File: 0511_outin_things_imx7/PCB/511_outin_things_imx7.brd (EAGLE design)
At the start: 85 x 56 mm, 57 parts

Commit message: Update for android things.
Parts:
- moved JP1 1.27 mm to (52.1, 37.0)
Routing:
- net 5V: track 275.3 -> 303.2 mm, vias 1 -> 0
- net N$7: track 35.5 -> 61.2 mm, vias 2 -> 0
- net GND: track 356.1 -> 375.5 mm, vias 21 -> 10
- net LED5: track 17.7 -> 36.1 mm, vias 2 -> 0
- net N$14: track 42.4 -> 28.5 mm, vias 2 -> 4
- net MOSI: track 37.1 -> 50.2 mm
- net SDA: track 62.9 -> 54.4 mm, vias 1 -> 0
- net CH1: track 31.7 -> 39.5 mm
- net MISO: track 45.4 -> 39.5 mm, vias 0 -> 1
- net I2S_SDOUT: track 40.5 -> 34.9 mm
- net CH0: track 40.1 -> 43.4 mm
- net SCL: track 49.0 -> 52.0 mm
- net LED3: track 14.7 -> 17.6 mm, vias 0 -> 2
- net SCLK: track 45.0 -> 42.3 mm
- net I2S_SDIN: track 29.8 -> 32.4 mm
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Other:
- board text added: "Rev.1.0.0D"
- board text removed: "Rev.1.0.0 C"

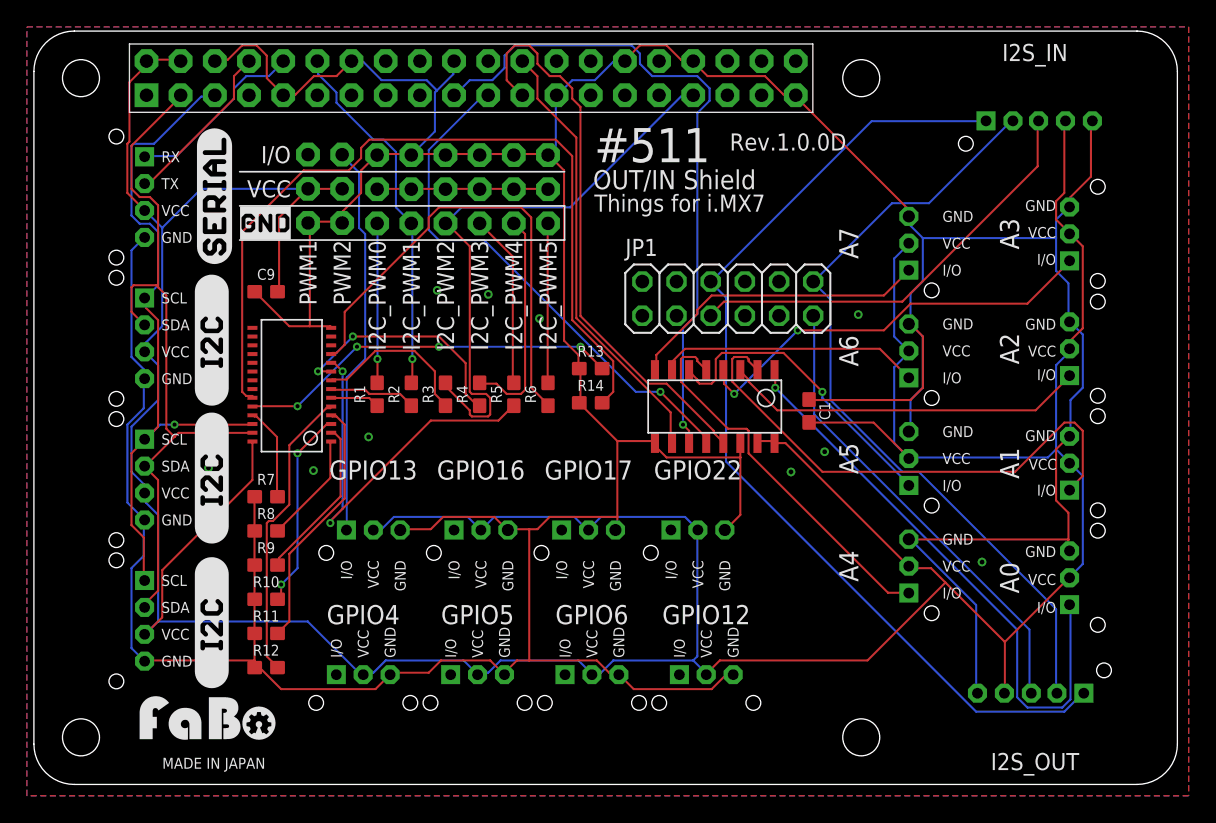
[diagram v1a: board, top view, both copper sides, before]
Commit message: #511 outin_things_imx7　ロゴ修正
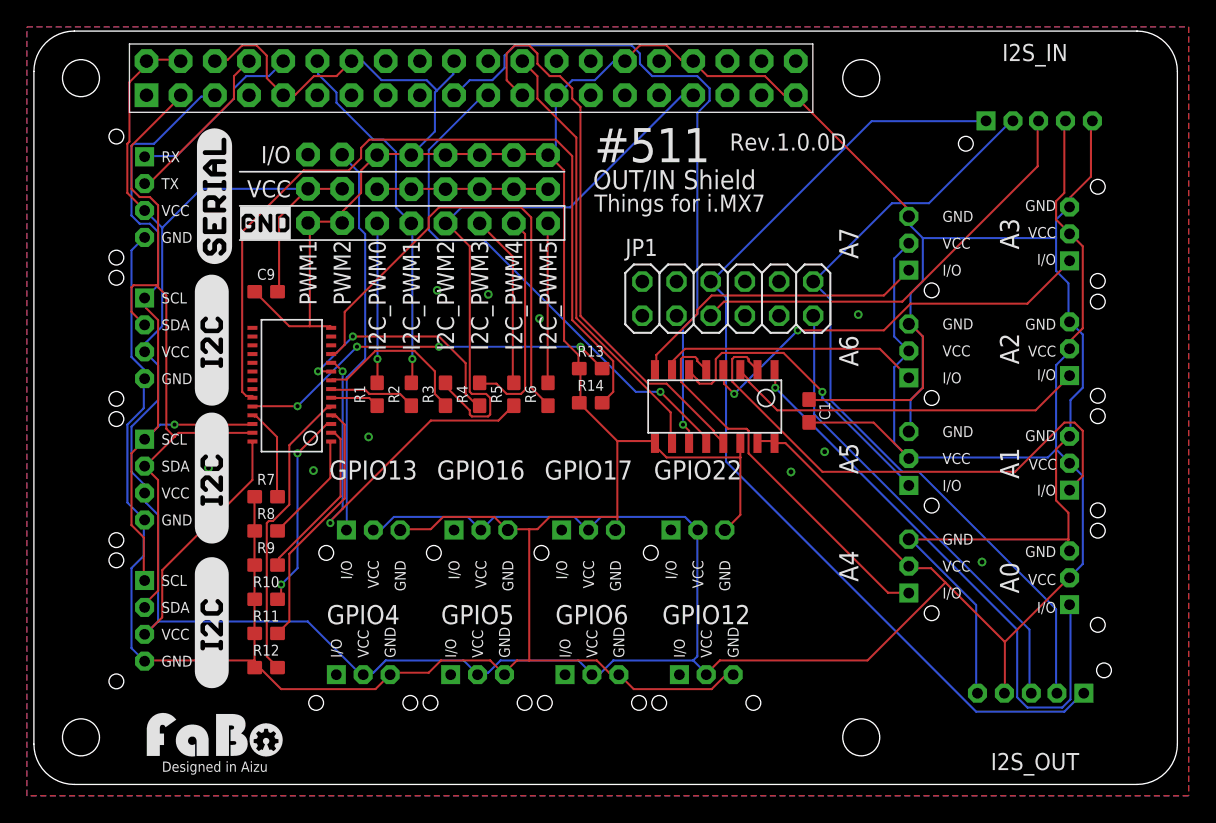
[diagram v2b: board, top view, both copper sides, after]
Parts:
- removed U$14: (no value), FaBo-etc:LOGO_FABO_MS
- added LOGO1: (no value), component:LOGO_FABO_M
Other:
- board text added: "Designed in Aizu"
- board text removed: "MADE IN JAPAN"
